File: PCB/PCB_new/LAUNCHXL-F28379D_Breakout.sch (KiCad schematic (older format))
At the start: 23 parts, among them IC1 LM358N, Q1 220mA/50V/3.5Ω, Q2 100V/17A, Q3 100V/17A, Q4 100V/17A, Q5 100V/17A, Q6 100V/17A

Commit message: cleaned up schematic
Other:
- note removed: "Connector to Servo Motor"
- note removed: "Drivetrain_control:1X06_LONGPADS"
- note removed: "Info from past connector\nDrivetrain_control:22-23-2041\nPCB_2020-rescue:22-23-2041-Drivetrain_control-eagle-import"
- note removed: "check size of molex connector"
- note removed: "check the package for this, needs to be SIL??\nSparkfun product specs"
- moved on the sheet: CONN6, CONN7
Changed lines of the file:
@@
 Wire Wire Line
 	10300 1700 10200 1700
-Text Label 5600 3500 0    70   ~ 0
-THROTTLE_MC
 Text Label 10950 4650 2    39   ~ 0
 THROTTLE_MC
@@
 Wire Wire Line
 	3000 1200 2900 1200
-Text Label 6000 1700 0    70   ~ 0
-INPUT_B+
 Wire Wire Line
 	3000 1100 1900 1100
@@
 Wire Wire Line
 	10200 1700 10200 1900
-Text Notes 2250 750  0    50   ~ 10
-check size of molex connector
-Text Notes 2700 2100 0    59   ~ 0
-Connector to Servo Motor
 $Comp
 L Connector:Conn_01x04_Male CONN5
@@
 	-1   0    0    1
 $EndComp
-Text Notes 10900 4950 0    50   ~ 10
-Info from past connector\nDrivetrain_control:22-23-2041\nPCB_2020-rescue:22-23-2041-Drivetrain_control-eagle-import
 Text Label 10950 4450 2    39   ~ 0
 FWD_MC
@@
 NoConn ~ 2000 3300
 NoConn ~ 2000 3700
-Text Notes 950  4550 0    50   ~ 0
-Drivetrain_control:1X06_LONGPADS
-Text Notes 1500 4450 0    50   ~ 0
-check the package for this, needs to be SIL??\nSparkfun product specs
 $Comp
 L Connector:Conn_01x08_Male CONN2
@@
 F 1 "SERVO_CONN" H 3172 1373 50  0000 R CNN
 F 2 "Connector_Molex:Molex_Mini-Fit_Jr_5566-08A2_2x04_P4.20mm_Vertical" H 3200 1400 50  0001 C CNN
-F 3 "https://www.molex.com/molex/products/datasheet.jsp?part=active/0039281083_PCB_HEADERS.xml" H 3200 1400 50  0001 C CNN
+F 3 "https://www.molex.com/molex/products/datasheet.jsp?part=active/0039288080_PCB_HEADERS.xml" H 3200 1400 50  0001 C CNN
 	1    3200 1400
 	-1   0    0    -1
@@
 L Connector:Conn_01x06_Male CONN6
 U 1 1 5E187579
-P 5250 6100
-F 0 "CONN6" H 5358 6481 50  0000 C CNN
-F 1 "Brake_MC_CONN" H 5358 6390 50  0000 C CNN
-F 2 "Drivetrain_control:Brake_MC_Conn" H 5250 6100 50  0001 C CNN
-F 3 "https://cdn-shop.adafruit.com/product-files/3190/drv8871.pdf" H 5250 6100 50  0001 C CNN
-F 4 "https://learn.adafruit.com/adafruit-drv8871-brushed-dc-motor-driver-breakout/" H 5250 6100 50  0001 C CNN "Website"
-	1    5250 6100
-	1    0    0    -1
-$EndComp
-Text GLabel 5450 5900 2    39   Input ~ 0
+P 2250 7600
+F 0 "CONN6" H 2358 7981 50  0000 C CNN
+F 1 "Brake_MC_CONN" H 2358 7890 50  0000 C CNN
+F 2 "Drivetrain_control:Brake_MC_Conn" H 2250 7600 50  0001 C CNN
+F 3 "https://cdn-shop.adafruit.com/product-files/3190/drv8871.pdf" H 2250 7600 50  0001 C CNN
+F 4 "https://learn.adafruit.com/adafruit-drv8871-brushed-dc-motor-driver-breakout/" H 2250 7600 50  0001 C CNN "Website"
+	1    2250 7600
+	1    0    0    -1
+$EndComp
+Text GLabel 2450 7400 2    39   Input ~ 0
 Brake_PWM_2
-Text GLabel 5450 6000 2    39   Input ~ 0
+Text GLabel 2450 7500 2    39   Input ~ 0
 Brake_PWM_1
 $Comp
 L power:GND #GND?
 U 1 1 5E188E1D
-P 6100 6250
+P 3100 7750
 AR Path="/5E188E1D" Ref="#GND?"  Part="1"
 AR Path="/5DD5E236/5E188E1D" Ref="#GND?"  Part="1"
 AR Path="/5DF27AC1/5E188E1D" Ref="#GND0101"  Part="1"
-F 0 "#GND0101" H 6100 6250 50  0001 C CNN
-F 1 "GND" H 6000 6050 59  0000 L BNN
-F 2 "" H 6100 6250 50  0001 C CNN
-F 3 "" H 6100 6250 50  0001 C CNN
-	1    6100 6250
+F 0 "#GND0101" H 3100 7750 50  0001 C CNN
+F 1 "GND" H 3000 7550 59  0000 L BNN
+F 2 "" H 3100 7750 50  0001 C CNN
+F 3 "" H 3100 7750 50  0001 C CNN
+	1    3100 7750
 	1    0    0    -1
 $EndComp
@@
 L power:+12V #P+?
 U 1 1 5E189D98
-P 6100 6050
+P 3100 7550
 AR Path="/5E189D98" Ref="#P+?"  Part="1"
 AR Path="/5DD5E236/5E189D98" Ref="#P+?"  Part="1"
 AR Path="/5DF27AC1/5E189D98" Ref="#P+0101"  Part="1"
-F 0 "#P+0101" H 6100 6050 50  0001 C CNN
-F 1 "+12V" H 6000 6200 59  0000 L BNN
-F 2 "" H 6100 6050 50  0001 C CNN
-F 3 "" H 6100 6050 50  0001 C CNN
-	1    6100 6050
-	1    0    0    -1
-$EndComp
-Wire Wire Line
-	5450 6100 6100 6100
-Wire Wire Line
-	6100 6100 6100 6050
-Wire Wire Line
-	5450 6200 6100 6200
-Wire Wire Line
-	6100 6200 6100 6250
-Text Label 5450 6300 0    39   ~ 0
+F 0 "#P+0101" H 3100 7550 50  0001 C CNN
+F 1 "+12V" H 3000 7700 59  0000 L BNN
+F 2 "" H 3100 7550 50  0001 C CNN
+F 3 "" H 3100 7550 50  0001 C CNN
+	1    3100 7550
+	1    0    0    -1
+$EndComp
+Wire Wire Line
+	2450 7600 3100 7600
+Wire Wire Line
+	3100 7600 3100 7550
+Wire Wire Line
+	2450 7700 3100 7700
+Wire Wire Line
+	3100 7700 3100 7750
+Text Label 2450 7800 0    39   ~ 0
 Brake_Out_1
-Text Label 5450 6400 0    39   ~ 0
+Text Label 2450 7900 0    39   ~ 0
 Brake_Out_2
-Text Label 7100 6150 2    39   ~ 0
+Text Label 4100 7650 2    39   ~ 0
 Brake_Out_1
-Text Label 7100 6250 2    39   ~ 0
+Text Label 4100 7750 2    39   ~ 0
 Brake_Out_2
 $Comp
 L Connector:Conn_01x02_Male CONN7
 U 1 1 5E1945B9
-P 7300 6250
-F 0 "CONN7" H 7272 6132 50  0000 R CNN
-F 1 "Brake_CONN" H 7272 6223 50  0000 R CNN
-F 2 "Connector_Molex:Molex_KK-254_AE-6410-02A_1x02_P2.54mm_Vertical" H 7300 6250 50  0001 C CNN
-F 3 "https://www.molex.com/molex/products/datasheet.jsp?part=active/0022272021_PCB_HEADERS.xml" H 7300 6250 50  0001 C CNN
-	1    7300 6250
+P 4300 7750
+F 0 "CONN7" H 4272 7632 50  0000 R CNN
+F 1 "Brake_CONN" H 4272 7723 50  0000 R CNN
+F 2 "Connector_Molex:Molex_KK-254_AE-6410-02A_1x02_P2.54mm_Vertical" H 4300 7750 50  0001 C CNN
+F 3 "https://www.molex.com/molex/products/datasheet.jsp?part=active/0022272021_PCB_HEADERS.xml" H 4300 7750 50  0001 C CNN
+	1    4300 7750
 	-1   0    0    1
 $EndComp
@@
 Text Notes 4950 5100 2    39   ~ 0
 These resistors are chosen to get 10/3 gain
+Text Label 6000 1700 0    70   ~ 0
+INPUT_B+
+Text Label 5600 3500 0    70   ~ 0
+THROTTLE_MC
 $EndSCHEMATC

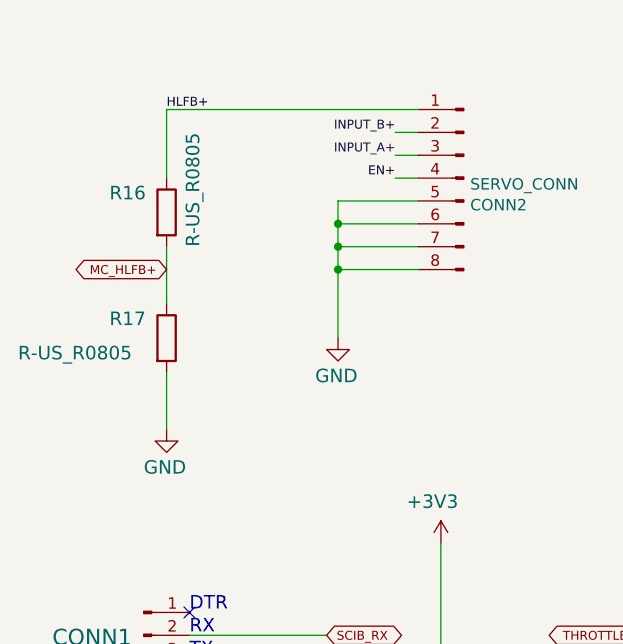
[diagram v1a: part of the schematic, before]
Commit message: removed signals to HLFB+ for steering motor
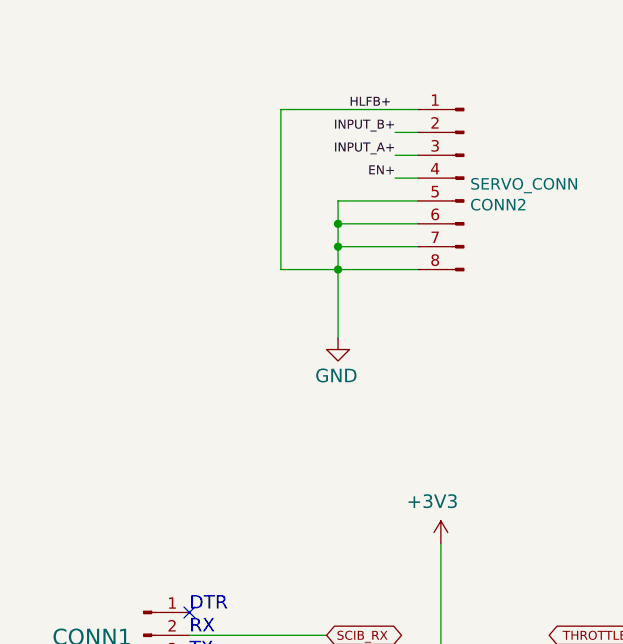
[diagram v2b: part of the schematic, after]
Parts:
- removed R16, R17: R-US_R0805, Resistor_SMD:R_0805_2012Metric_Pad1.15x1.40mm_HandSolder, symbol Device:R
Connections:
- net labels removed: MC_HLFB+
- wire segments 77 -> 76
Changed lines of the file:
@@
 Wire Wire Line
 	3000 1200 2900 1200
-Wire Wire Line
-	3000 1100 1900 1100
-Wire Wire Line
-	1900 1100 1900 1400
-Text Label 1900 1100 0    39   ~ 0
+Text Label 2700 1100 0    39   ~ 0
 HLFB+
 Wire Wire Line
@@
 Text GLabel 10800 3200 3    39   BiDi ~ 0
 FS1_CTL
-Text GLabel 1900 1800 0    39   BiDi ~ 0
-MC_HLFB+
 Text GLabel 7500 3200 3    39   BiDi ~ 0
 INPUT_A+_CTL
@@
 F 3 "" H 2650 2100 50  0001 C CNN
 	1    2650 2100
-	1    0    0    -1
-$EndComp
-$Comp
-L power:GND #GND17
-U 1 1 D1FA1B5E
-P 1900 2500
-AR Path="/D1FA1B5E" Ref="#GND17"  Part="1"
-AR Path="/5DD5E236/D1FA1B5E" Ref="#GND17"  Part="1"
-AR Path="/5DF27AC1/D1FA1B5E" Ref="#GND017"  Part="1"
-F 0 "#GND017" H 1900 2500 50  0001 C CNN
-F 1 "GND" H 1800 2300 59  0000 L BNN
-F 2 "" H 1900 2500 50  0001 C CNN
-F 3 "" H 1900 2500 50  0001 C CNN
-	1    1900 2500
 	1    0    0    -1
 $EndComp
@@
 Wire Wire Line
 	4500 1700 4800 1700
-$Comp
-L Device:R R16
-U 1 1 7A1EFB6B
-P 1900 1550
-AR Path="/7A1EFB6B" Ref="R16"  Part="1"
-AR Path="/5DD5E236/7A1EFB6B" Ref="R16"  Part="1"
-AR Path="/5DF27AC1/7A1EFB6B" Ref="R16"  Part="1"
-F 0 "R16" H 1650 1600 59  0000 L BNN
-F 1 "R-US_R0805" V 2050 1400 59  0000 L BNN
-F 2 "Resistor_SMD:R_0805_2012Metric_Pad1.15x1.40mm_HandSolder" H 1900 1550 50  0001 C CNN
-F 3 "" H 1900 1550 50  0001 C CNN
-	1    1900 1550
-	1    0    0    -1
-$EndComp
-Wire Wire Line
-	1900 1700 1900 1950
-$Comp
-L Device:R R17
-U 1 1 902AE53C
-P 1900 2100
-AR Path="/902AE53C" Ref="R17"  Part="1"
-AR Path="/5DD5E236/902AE53C" Ref="R17"  Part="1"
-AR Path="/5DF27AC1/902AE53C" Ref="R17"  Part="1"
-F 0 "R17" H 1650 2150 59  0000 L BNN
-F 1 "R-US_R0805" H 1250 2000 59  0000 L BNN
-F 2 "Resistor_SMD:R_0805_2012Metric_Pad1.15x1.40mm_HandSolder" H 1900 2100 50  0001 C CNN
-F 3 "" H 1900 2100 50  0001 C CNN
-	1    1900 2100
-	1    0    0    -1
-$EndComp
-Wire Wire Line
-	1900 2250 1900 2500
 Text Label 2900 1200 2    39   ~ 0
 INPUT_B+
@@
 Text Label 5600 3500 0    70   ~ 0
 THROTTLE_MC
+Wire Wire Line
+	3000 1100 2400 1100
+Wire Wire Line
+	2400 1100 2400 1800
+Wire Wire Line
+	2400 1800 2650 1800
 $EndSCHEMATC

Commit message: added 3 to 12 volt conversion circuit for braking PWM
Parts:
- added Q7, Q8: 220mA/50V/3.5Ω, Package_TO_SOT_SMD:SOT-23, symbol Device:Q_NMOS_GSD
- added R6, R7, R8, R9: 10k, Resistor_SMD:R_0805_2012Metric_Pad1.15x1.40mm_HandSolder, symbol Device:R
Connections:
- net labels added: Brake_Ctr_1, Brake_Ctr_2
- wire segments 76 -> 98
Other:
- note added: "NOTE: This Brake Conn is itself a\npass through from PWM input to output\n"
- moved on the sheet: CONN6, CONN7

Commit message: removed unneeded level shifters
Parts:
- removed Q7, Q8: 220mA/50V/3.5Ω, Package_TO_SOT_SMD:SOT-23, symbol Device:Q_NMOS_GSD
- removed R6, R7, R8, R9: 10k, Resistor_SMD:R_0805_2012Metric_Pad1.15x1.40mm_HandSolder, symbol Device:R
- CONN2: footprint Connector_Molex:Molex_Mini-Fit_Jr_5566-08A2_2x04_P4.20mm_Vertical -> Connector_Molex:Molex_Mini-Fit_Jr_5566-08A_2x04_P4.20mm_Vertical
- CONN6: footprint Drivetrain_control:Brake_MC_Conn -> Drivetrain_control:Brake_MC_Conn_6pin
- CONN7: footprint Connector_Molex:Molex_KK-254_AE-6410-02A_1x02_P2.54mm_Vertical -> Connector_Molex:Molex_Mini-Fit_Jr_5566-02A_2x01_P4.20mm_Vertical
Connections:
- net labels removed: Brake_Ctr_1, Brake_Ctr_2
- wire segments 98 -> 76
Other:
- moved on the sheet: CONN7
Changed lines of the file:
@@
 F 0 "CONN2" H 3172 1282 50  0000 R CNN
 F 1 "SERVO_CONN" H 3172 1373 50  0000 R CNN
-F 2 "Connector_Molex:Molex_Mini-Fit_Jr_5566-08A2_2x04_P4.20mm_Vertical" H 3200 1400 50  0001 C CNN
+F 2 "Connector_Molex:Molex_Mini-Fit_Jr_5566-08A_2x04_P4.20mm_Vertical" H 3200 1400 50  0001 C CNN
 F 3 "https://www.molex.com/molex/products/datasheet.jsp?part=active/0039288080_PCB_HEADERS.xml" H 3200 1400 50  0001 C CNN
 	1    3200 1400
@@
 F 0 "CONN6" H 1558 7831 50  0000 C CNN
 F 1 "Brake_MC_CONN" H 1558 7740 50  0000 C CNN
-F 2 "Drivetrain_control:Brake_MC_Conn" H 1450 7450 50  0001 C CNN
+F 2 "Drivetrain_control:Brake_MC_Conn_6pin" H 1450 7450 50  0001 C CNN
 F 3 "https://cdn-shop.adafruit.com/product-files/3190/drv8871.pdf" H 1450 7450 50  0001 C CNN
 F 4 "https://learn.adafruit.com/adafruit-drv8871-brushed-dc-motor-driver-breakout/" H 1450 7450 50  0001 C CNN "Website"
@@
 	1    0    0    -1
 $EndComp
-Text GLabel 3850 8600 0    39   Input ~ 0
+Text GLabel 1650 7250 2    39   Input ~ 0
 Brake_PWM_2
-Text GLabel 3850 7050 0    39   Input ~ 0
+Text GLabel 1650 7350 2    39   Input ~ 0
 Brake_PWM_1
 $Comp
@@
 Wire Wire Line
 	2300 7550 2300 7600
-Text Label 5350 7050 0    39   ~ 0
-Brake_Ctr_1
-Text Label 5350 8600 0    39   ~ 0
-Brake_Ctr_2
 $Comp
 L Connector:Conn_01x02_Male CONN7
 U 1 1 5E1945B9
-P 6900 7600
-F 0 "CONN7" H 6872 7482 50  0000 R CNN
-F 1 "Brake_CONN" H 6872 7573 50  0000 R CNN
-F 2 "Connector_Molex:Molex_KK-254_AE-6410-02A_1x02_P2.54mm_Vertical" H 6900 7600 50  0001 C CNN
-F 3 "https://www.molex.com/molex/products/datasheet.jsp?part=active/0022272021_PCB_HEADERS.xml" H 6900 7600 50  0001 C CNN
-	1    6900 7600
+P 3600 7500
+F 0 "CONN7" H 3572 7382 50  0000 R CNN
+F 1 "Brake_CONN" H 3572 7473 50  0000 R CNN
+F 2 "Connector_Molex:Molex_Mini-Fit_Jr_5566-02A_2x01_P4.20mm_Vertical" H 3600 7500 50  0001 C CNN
+F 3 "https://www.molex.com/molex/products/datasheet.jsp?part=active/0022272021_PCB_HEADERS.xml" H 3600 7500 50  0001 C CNN
+	1    3600 7500
 	-1   0    0    1
 $EndComp
@@
 Wire Wire Line
 	2400 1800 2650 1800
-Wire Wire Line
-	4150 6650 4150 6450
-$Comp
-L Device:R R?
-U 1 1 5E1D7004
-P 4150 6850
-AR Path="/5E1D7004" Ref="R?"  Part="1"
-AR Path="/5DD5E236/5E1D7004" Ref="R?"  Part="1"
-AR Path="/5DF27AC1/5E1D7004" Ref="R6"  Part="1"
-F 0 "R6" H 3950 6900 59  0000 L BNN
-F 1 "10k" H 3900 6800 59  0000 L BNN
-F 2 "Resistor_SMD:R_0805_2012Metric_Pad1.15x1.40mm_HandSolder" H 4150 6850 50  0001 C CNN
-F 3 "" H 4150 6850 50  0001 C CNN
-	1    4150 6850
-	1    0    0    -1
-$EndComp
-$Comp
-L power:+3V3 #+3V?
-U 1 1 5E1D700E
-P 4150 6450
-AR Path="/5E1D700E" Ref="#+3V?"  Part="1"
-AR Path="/5DD5E236/5E1D700E" Ref="#+3V?"  Part="1"
-AR Path="/5DF27AC1/5E1D700E" Ref="#+3V03"  Part="1"
-F 0 "#+3V03" H 4150 6450 50  0001 C CNN
-F 1 "+3V3" H 4050 6600 59  0000 L BNN
-F 2 "" H 4150 6450 50  0001 C CNN
-F 3 "" H 4150 6450 50  0001 C CNN
-	1    4150 6450
-	1    0    0    -1
-$EndComp
-$Comp
-L power:+12V #P+?
-U 1 1 5E1D7018
-P 5150 6450
-AR Path="/5E1D7018" Ref="#P+?"  Part="1"
-AR Path="/5DD5E236/5E1D7018" Ref="#P+?"  Part="1"
-AR Path="/5DF27AC1/5E1D7018" Ref="#P+06"  Part="1"
-F 0 "#P+06" H 5150 6450 50  0001 C CNN
-F 1 "+12V" H 5050 6600 59  0000 L BNN
-F 2 "" H 5150 6450 50  0001 C CNN
-F 3 "" H 5150 6450 50  0001 C CNN
-	1    5150 6450
-	1    0    0    -1
-$EndComp
-Wire Wire Line
-	4850 7050 5150 7050
-Wire Wire Line
-	3850 7050 4150 7050
-Wire Wire Line
-	4150 6650 4150 6700
-Connection ~ 4150 6650
-Wire Wire Line
-	4150 7000 4150 7050
-Connection ~ 4150 7050
-Wire Wire Line
-	4150 7050 4450 7050
-Wire Wire Line
-	5150 6450 5150 6700
-Wire Wire Line
-	5150 7000 5150 7050
-Connection ~ 5150 7050
-Wire Wire Line
-	5150 7050 5350 7050
-Wire Wire Line
-	4650 6650 4650 6750
-Wire Wire Line
-	4150 6650 4650 6650
-$Comp
-L Device:R R?
-U 1 1 5E1D7030
-P 5150 6850
-AR Path="/5E1D7030" Ref="R?"  Part="1"
-AR Path="/5DD5E236/5E1D7030" Ref="R?"  Part="1"
-AR Path="/5DF27AC1/5E1D7030" Ref="R8"  Part="1"
-F 0 "R8" H 4950 6850 59  0000 L BNN
-F 1 "10k" H 4900 6750 59  0000 L BNN
-F 2 "Resistor_SMD:R_0805_2012Metric_Pad1.15x1.40mm_HandSolder" H 5150 6850 50  0001 C CNN
-F 3 "" H 5150 6850 50  0001 C CNN
-	1    5150 6850
-	1    0    0    -1
-$EndComp
-$Comp
-L Device:Q_NMOS_GSD Q?
-U 1 1 5E1D703A
-P 4650 6950
-AR Path="/5E1D703A" Ref="Q?"  Part="1"
-AR Path="/5DD5E236/5E1D703A" Ref="Q?"  Part="1"
-AR Path="/5DF27AC1/5E1D703A" Ref="Q7"  Part="1"
-F 0 "Q7" V 4950 6900 70  0000 L BNN
-F 1 "220mA/50V/3.5Ω" V 5050 6700 70  0000 L BNN
-F 2 "Package_TO_SOT_SMD:SOT-23" H 4650 6950 50  0001 C CNN
-F 3 "https://www.digikey.com/product-detail/en/on-semiconductor/BSS138-F085/BSS138-F085OSCT-ND/9086388" H 4650 6950 50  0001 C CNN
-	1    4650 6950
-	0    1    1    0
-$EndComp
-Wire Wire Line
-	4150 8200 4150 8000
-$Comp
-L Device:R R?
-U 1 1 5E1E4782
-P 4150 8400
-AR Path="/5E1E4782" Ref="R?"  Part="1"
-AR Path="/5DD5E236/5E1E4782" Ref="R?"  Part="1"
-AR Path="/5DF27AC1/5E1E4782" Ref="R7"  Part="1"
-F 0 "R7" H 3950 8450 59  0000 L BNN
-F 1 "10k" H 3900 8350 59  0000 L BNN
-F 2 "Resistor_SMD:R_0805_2012Metric_Pad1.15x1.40mm_HandSolder" H 4150 8400 50  0001 C CNN
-F 3 "" H 4150 8400 50  0001 C CNN
-	1    4150 8400
-	1    0    0    -1
-$EndComp
-$Comp
-L power:+3V3 #+3V?
-U 1 1 5E1E478C
-P 4150 8000
-AR Path="/5E1E478C" Ref="#+3V?"  Part="1"
-AR Path="/5DD5E236/5E1E478C" Ref="#+3V?"  Part="1"
-AR Path="/5DF27AC1/5E1E478C" Ref="#+3V05"  Part="1"
-F 0 "#+3V05" H 4150 8000 50  0001 C CNN
-F 1 "+3V3" H 4050 8150 59  0000 L BNN
-F 2 "" H 4150 8000 50  0001 C CNN
-F 3 "" H 4150 8000 50  0001 C CNN
-	1    4150 8000
-	1    0    0    -1
-$EndComp
-$Comp
-L power:+12V #P+?
-U 1 1 5E1E4796
-P 5150 8000
-AR Path="/5E1E4796" Ref="#P+?"  Part="1"
-AR Path="/5DD5E236/5E1E4796" Ref="#P+?"  Part="1"
-AR Path="/5DF27AC1/5E1E4796" Ref="#P+07"  Part="1"
-F 0 "#P+07" H 5150 8000 50  0001 C CNN
-F 1 "+12V" H 5050 8150 59  0000 L BNN
-F 2 "" H 5150 8000 50  0001 C CNN
-F 3 "" H 5150 8000 50  0001 C CNN
-	1    5150 8000
-	1    0    0    -1
-$EndComp
-Wire Wire Line
-	4850 8600 5150 8600
-Wire Wire Line
-	3850 8600 4150 8600
-Wire Wire Line
-	4150 8200 4150 8250
-Connection ~ 4150 8200
-Wire Wire Line
-	4150 8550 4150 8600
-Connection ~ 4150 8600
-Wire Wire Line
-	4150 8600 4450 8600
-Wire Wire Line
-	5150 8000 5150 8250
-Wire Wire Line
-	5150 8550 5150 8600
-Connection ~ 5150 8600
-Wire Wire Line
-	5150 8600 5350 8600
-Wire Wire Line
-	4650 8200 4650 8300
-Wire Wire Line
-	4150 8200 4650 8200
-$Comp
-L Device:R R?
-U 1 1 5E1E47AE
-P 5150 8400
-AR Path="/5E1E47AE" Ref="R?"  Part="1"
-AR Path="/5DD5E236/5E1E47AE" Ref="R?"  Part="1"
-AR Path="/5DF27AC1/5E1E47AE" Ref="R9"  Part="1"
-F 0 "R9" H 4950 8400 59  0000 L BNN
-F 1 "10k" H 4900 8300 59  0000 L BNN
-F 2 "Resistor_SMD:R_0805_2012Metric_Pad1.15x1.40mm_HandSolder" H 5150 8400 50  0001 C CNN
-F 3 "" H 5150 8400 50  0001 C CNN
-	1    5150 8400
-	1    0    0    -1
-$EndComp
-$Comp
-L Device:Q_NMOS_GSD Q?
-U 1 1 5E1E47B8
-P 4650 8500
-AR Path="/5E1E47B8" Ref="Q?"  Part="1"
-AR Path="/5DD5E236/5E1E47B8" Ref="Q?"  Part="1"
-AR Path="/5DF27AC1/5E1E47B8" Ref="Q8"  Part="1"
-F 0 "Q8" V 4950 8450 70  0000 L BNN
-F 1 "220mA/50V/3.5Ω" V 5050 8250 70  0000 L BNN
-F 2 "Package_TO_SOT_SMD:SOT-23" H 4650 8500 50  0001 C CNN
-F 3 "https://www.digikey.com/product-detail/en/on-semiconductor/BSS138-F085/BSS138-F085OSCT-ND/9086388" H 4650 8500 50  0001 C CNN
-	1    4650 8500
-	0    1    1    0
-$EndComp
-Text Label 6700 7500 2    39   ~ 0
+Text Label 3400 7400 2    39   ~ 0
 Brake_Out_1
 Text Label 1650 7650 0    39   ~ 0
 Brake_Out_1
-Text Label 6700 7600 2    39   ~ 0
+Text Label 3400 7500 2    39   ~ 0
 Brake_Out_2
 Text Label 1650 7750 0    39   ~ 0
@@
 Text Notes 1200 8200 0    50   ~ 0
 NOTE: This Brake Conn is itself a\npass through from PWM input to output\n
-Text Label 1650 7250 0    39   ~ 0
-Brake_Ctr_2
-Text Label 1650 7350 0    39   ~ 0
-Brake_Ctr_1
 $EndSCHEMATC

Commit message: changed mosfet type and package for level shifter circuit
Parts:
- removed Q1: 220mA/50V/3.5Ω, Package_TO_SOT_SMD:SOT-23, symbol Device:Q_NMOS_GSD
- added Q1: 100V/17A, Package_TO_SOT_THT:TO-220-3_Vertical, symbol Device:Q_NMOS_GDS
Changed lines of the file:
@@
 	-1   0    0    -1
-$EndComp
-$Comp
-L Device:Q_NMOS_GSD Q1
-U 1 1 A1BE61D0
-P 5300 1600
-AR Path="/A1BE61D0" Ref="Q1"  Part="1"
-AR Path="/5DD5E236/A1BE61D0" Ref="Q1"  Part="1"
-AR Path="/5DF27AC1/A1BE61D0" Ref="Q1"  Part="1"
-F 0 "Q1" V 5600 1550 70  0000 L BNN
-F 1 "220mA/50V/3.5Ω" V 5700 1350 70  0000 L BNN
-F 2 "Package_TO_SOT_SMD:SOT-23" H 5300 1600 50  0001 C CNN
-F 3 "https://www.digikey.com/product-detail/en/on-semiconductor/BSS138-F085/BSS138-F085OSCT-ND/9086388" H 5300 1600 50  0001 C CNN
-	1    5300 1600
-	0    1    1    0
 $EndComp
 Wire Wire Line
@@
 Text Notes 1200 8200 0    50   ~ 0
 NOTE: This Brake Conn is itself a\npass through from PWM input to output\n
+$Comp
+L Device:Q_NMOS_GDS Q?
+U 1 1 5E250E23
+P 5300 1600
+AR Path="/5E250E23" Ref="Q?"  Part="1"
+AR Path="/5DD5E236/5E250E23" Ref="Q?"  Part="1"
+AR Path="/5DF27AC1/5E250E23" Ref="Q1"  Part="1"
+F 0 "Q1" V 5600 1500 70  0000 L BNN
+F 1 "100V/17A" V 5700 1350 70  0000 L BNN
+F 2 "Package_TO_SOT_THT:TO-220-3_Vertical" H 5300 1600 50  0001 C CNN
+F 3 "https://www.infineon.com/dgdl/irl530npbf.pdf?fileId=5546d462533600a40153565fad5c2560" H 5300 1600 50  0001 C CNN
+	1    5300 1600
+	0    1    1    0
+$EndComp
 $EndSCHEMATC
